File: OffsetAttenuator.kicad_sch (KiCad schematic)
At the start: 15 parts, among them J1 Conn_Coaxial, J2 Conn_Coaxial, SW1 SW_SPST, U1 L7805, X1 CXO_DIP14

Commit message: updating schematic
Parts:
- added D2: LED, symbol Device:LED
- added R5: 220, symbol Device:R
- BT1: value Battery -> Battery 9V
- C1, C2: value C -> 470pF
- C3: value C -> .0047uF
- R1, R3: value R -> 2.2K
- R4: value R -> 4.7K
- RV1: value R_Potentiometer -> 5K
- X1: value CXO_DIP14 -> 4MHz
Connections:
- net GND: now also D2.1 (K)
- net +5V: now reaches U1.3 (OUT), X1.14 (Vcc)
- net +5V: now also R5.2
- net at R4.1, SW1.2 (B): now also U1.1 (IN)
- new net: D2.2 (A), R5.1
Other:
- note added: "Circuit borrowed from this project: https://www.w9dup.org/test_eqpt_files/attenuator_project_2010_may.pdf"

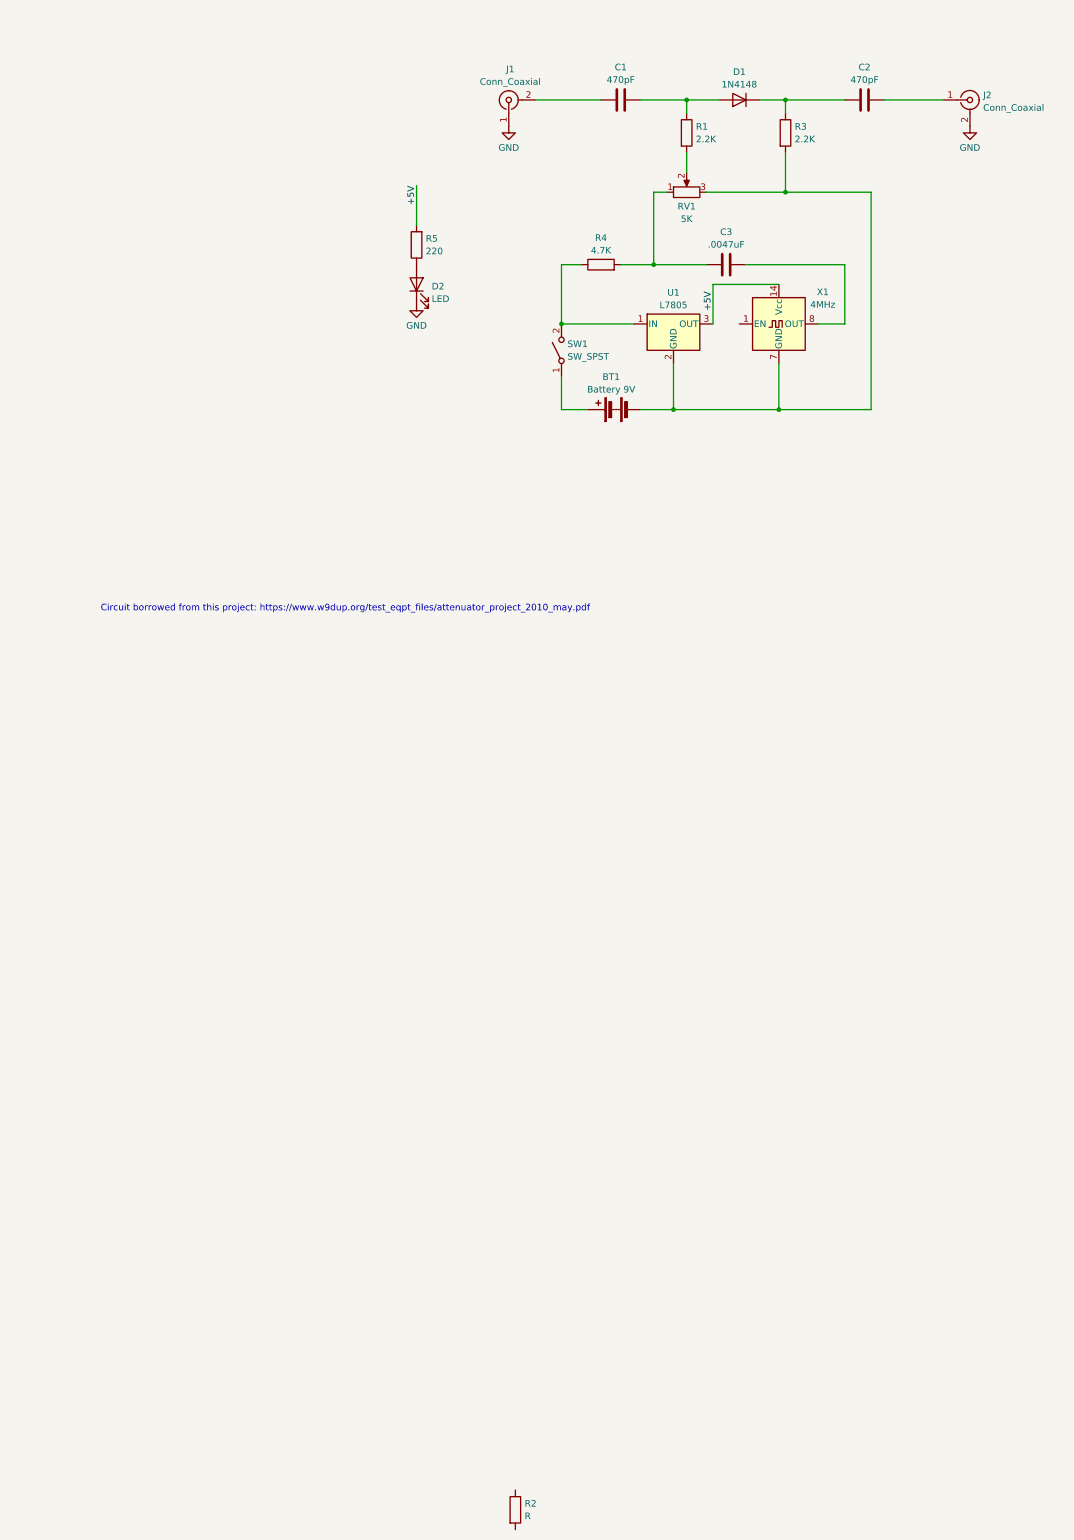
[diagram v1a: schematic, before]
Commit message: adding bypass toggle
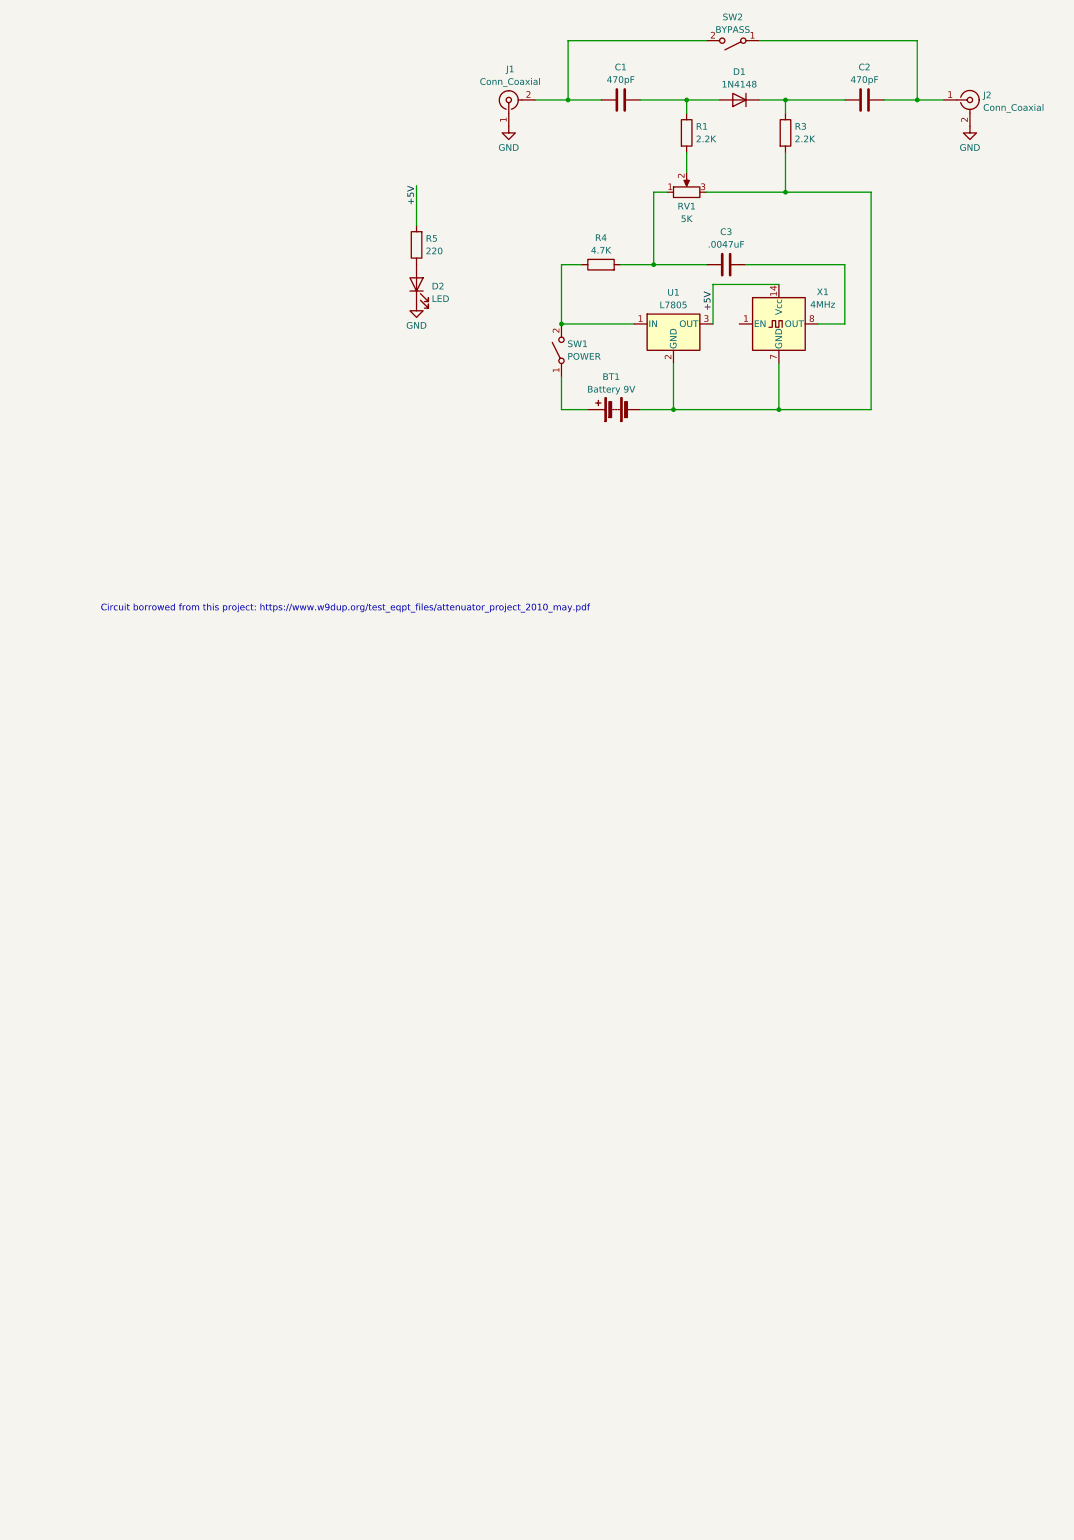
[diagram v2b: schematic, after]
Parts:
- removed R2: R, symbol Device:R
- added SW2: BYPASS, symbol Switch:SW_SPST
- SW1: value SW_SPST -> POWER
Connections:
- net at C2.2, J2.1 (In): now also SW2.1 (A)
- net at C1.1, J1.2 (Ext): now also SW2.2 (B)
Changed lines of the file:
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@@
+	)
+	(junction
+		(at 110.49 95.25)
+		(diameter 0)
+		(color 0 0 0 0)
 	)
 	(junction
@@
 	)
 	(junction
+		(at 177.8 95.25)
+		(diameter 0)
+		(color 0 0 0 0)
+	)
+	(junction
 		(at 151.13 154.94)
 		(diameter 0)
@@
 	(wire
 		(pts
+			(xy 137.16 83.82) (xy 110.49 83.82)
+		)
+		(stroke
+			(width 0)
+			(type default)
+		)
+	)
+	(wire
+		(pts
+			(xy 177.8 95.25) (xy 182.88 95.25)
+		)
+		(stroke
+			(width 0)
+			(type default)
+		)
+	)
+	(wire
+		(pts
 			(xy 127 127) (xy 137.16 127)
 		)
@@
 	(wire
 		(pts
-			(xy 104.14 95.25) (xy 116.84 95.25)
+			(xy 104.14 95.25) (xy 110.49 95.25)
 		)
 		(stroke
@@
 	(wire
 		(pts
+			(xy 110.49 95.25) (xy 116.84 95.25)
+		)
+		(stroke
+			(width 0)
+			(type default)
+		)
+	)
+	(wire
+		(pts
 			(xy 113.03 127) (xy 109.22 127)
 		)
@@
 	(wire
 		(pts
-			(xy 171.45 95.25) (xy 182.88 95.25)
+			(xy 177.8 83.82) (xy 177.8 95.25)
+		)
+		(stroke
+			(width 0)
+			(type default)
+		)
+	)
+	(wire
+		(pts
+			(xy 171.45 95.25) (xy 177.8 95.25)
 		)
 		(stroke
@@
 	(wire
 		(pts
+			(xy 147.32 83.82) (xy 177.8 83.82)
+		)
+		(stroke
+			(width 0)
+			(type default)
+		)
+	)
+	(wire
+		(pts
 			(xy 127 113.03) (xy 127 127)
 		)
@@
 		(pts
 			(xy 151.13 154.94) (xy 168.91 154.94)
+		)
+		(stroke
+			(width 0)
+			(type default)
+		)
+	)
+	(wire
+		(pts
+			(xy 110.49 83.82) (xy 110.49 95.25)
 		)
 		(stroke
@@
 	)
 	(symbol
+		(lib_id "Switch:SW_SPST")
+		(at 142.24 83.82 180)
+		(unit 1)
+		(exclude_from_sim no)
+		(in_bom yes)
+		(on_board yes)
+		(dnp no)
+		(fields_autoplaced yes)
+		(property "Reference" "SW2"
+			(at 142.24 79.2945 0)
+			(effects
+				(font
+					(size 1.27 1.27)
+				)
+			)
+		)
+		(property "Value" "BYPASS"
+			(at 142.24 81.7188 0)
+			(effects
+				(font
+					(size 1.27 1.27)
+				)
+			)
+		)
+		(property "Footprint" ""
+			(at 142.24 83.82 0)
+			(effects
+				(font
+					(size 1.27 1.27)
+				)
+				(hide yes)
+			)
+		)
+		(property "Datasheet" "~"
+			(at 142.24 83.82 0)
+			(effects
+				(font
+					(size 1.27 1.27)
+				)
+				(hide yes)
+			)
+		)
+		(property "Description" "Single Pole Single Throw (SPST) switch"
+			(at 142.24 83.82 0)
+			(effects
+				(font
+					(size 1.27 1.27)
+				)
+				(hide yes)
+			)
+		)
+		(pin "2"
+		)
+		(pin "1"
+		)
+		(instances
+			(project "OffsetAttenuator"
+				(path "/1ad55a5d-7440-488e-8560-ee9e41fda5dc"
+					(reference "SW2")
+					(unit 1)
+				)
+			)
+		)
+	)
+	(symbol
 		(lib_id "Regulator_Linear:L7805")
 		(at 130.81 138.43 0)
@@
 			)
 		)
-		(property "Value" "SW_SPST"
+		(property "Value" "POWER"
 			(at 110.363 144.7221 90)
 			(effects
@@
 					(unit 1)
 				)
-			)
-		)
-	)
-	(symbol
-		(lib_id "Device:R")
-		(at 100.33 367.03 0)
-		(unit 1)
-		(exclude_from_sim no)
-		(in_bom yes)
-		(on_board yes)
-		(dnp no)
-		(fields_autoplaced yes)
-		(property "Reference" "R2"
-			(at 102.108 365.8178 0)
-			(effects
-				(font
-					(size 1.27 1.27)
-				)
-				(justify left)
-			)
-		)
-		(property "Value" "R"
-			(at 102.108 368.2421 0)
-			(effects
-				(font
-					(size 1.27 1.27)
-				)
-				(justify left)
-			)
-		)
-		(property "Footprint" ""
-			(at 98.552 367.03 90)
-			(effects
-				(font
-					(size 1.27 1.27)
-				)
-				(hide yes)
-			)
-		)
-		(property "Datasheet" "~"
-			(at 100.33 367.03 0)
-			(effects
-				(font
-					(size 1.27 1.27)
-				)
-				(hide yes)
-			)
-		)
-		(property "Description" "Resistor"
-			(at 100.33 367.03 0)
-			(effects
-				(font
-					(size 1.27 1.27)
-				)
-				(hide yes)
-			)
-		)
-		(pin "2"
-		)
-		(pin "1"
-		)
-		(instances
-			(project "OffsetAttenuator"
-				(path "/1ad55a5d-7440-488e-8560-ee9e41fda5dc"
-					(reference "R2")
-					(unit 1)
-				)

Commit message: assigning footprints
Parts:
- BT1: footprint (none) -> Connector_PinHeader_2.54mm:PinHeader_1x02_P2.54mm_Vertical
- C1, C2, C3: footprint (none) -> Capacitor_THT:C_Disc_D5.0mm_W2.5mm_P5.00mm
- D2: footprint (none) -> LED_THT:LED_D5.0mm
- J1, J2: footprint (none) -> Library:CONBNC002
- R1, R3, R4, R5: footprint (none) -> Resistor_THT:R_Axial_DIN0309_L9.0mm_D3.2mm_P12.70mm_Horizontal
- U1: footprint (none) -> Package_TO_SOT_THT:TO-220-3_Vertical
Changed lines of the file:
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@@
 			)
 		)
-		(property "Footprint" ""
+		(property "Footprint" "LED_THT:LED_D5.0mm"
 			(at 81.28 130.81 0)
 			(effects
@@
 			)
 		)
-		(property "Footprint" ""
+		(property "Footprint" "Resistor_THT:R_Axial_DIN0309_L9.0mm_D3.2mm_P12.70mm_Horizontal"
 			(at 83.058 123.19 90)
 			(effects
@@
 			)
 		)
-		(property "Footprint" ""
+		(property "Footprint" "Resistor_THT:R_Axial_DIN0309_L9.0mm_D3.2mm_P12.70mm_Horizontal"
 			(at 150.622 101.6 90)
 			(effects
@@
 			)
 		)
-		(property "Footprint" ""
+		(property "Footprint" "Capacitor_THT:C_Disc_D5.0mm_W2.5mm_P5.00mm"
 			(at 144.78 126.0348 0)
 			(effects
@@
 			)
 		)
-		(property "Footprint" ""
+		(property "Footprint" "Capacitor_THT:C_Disc_D5.0mm_W2.5mm_P5.00mm"
 			(at 171.45 94.2848 0)
 			(effects
@@
 			)
 		)
-		(property "Footprint" ""
+		(property "Footprint" "Connector_PinHeader_2.54mm:PinHeader_1x02_P2.54mm_Vertical"
 			(at 117.856 154.94 90)
 			(effects
@@
 			)
 		)
-		(property "Footprint" ""
+		(property "Footprint" "Resistor_THT:R_Axial_DIN0309_L9.0mm_D3.2mm_P12.70mm_Horizontal"
 			(at 116.84 128.778 90)
 			(effects
@@
 			)
 		)
-		(property "Footprint" ""
+		(property "Footprint" "Library:CONBNC002"
 			(at 99.06 95.25 0)
 			(effects
@@
 			)
 		)
-		(property "Footprint" ""
+		(property "Footprint" "Resistor_THT:R_Axial_DIN0309_L9.0mm_D3.2mm_P12.70mm_Horizontal"
 			(at 131.572 101.6 90)
 			(effects
@@
 			)
 		)
-		(property "Footprint" ""
+		(property "Footprint" "Capacitor_THT:C_Disc_D5.0mm_W2.5mm_P5.00mm"
 			(at 124.46 94.2848 0)
 			(effects
@@
 			)
 		)
-		(property "Footprint" ""
+		(property "Footprint" "Package_TO_SOT_THT:TO-220-3_Vertical"
 			(at 131.445 142.24 0)
 			(effects
@@
 			)
 		)
-		(property "Footprint" ""
+		(property "Footprint" "Library:CONBNC002"
 			(at 187.96 95.25 0)
 			(effects

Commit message: upgrading to kicad 9
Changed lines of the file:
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@@
 (kicad_sch
-	(version 20231120)
+	(version 20250114)
 	(generator "eeschema")
-	(generator_version "8.0")
+	(generator_version "9.0")
 	(paper "A4")
+	(text "Circuit borrowed from this project: https://www.w9dup.org/test_eqpt_files/attenuator_project_2010_may.pdf"
+		(exclude_from_sim no)
+		(at 67.564 193.294 0)
+		(effects
+			(font
+				(size 1.27 1.27)
+			)
+		)
+	)
 	(junction
 		(at 133.35 95.25)
@@
 		)
 	)
-	(text "Circuit borrowed from this project: https://www.w9dup.org/test_eqpt_files/attenuator_project_2010_may.pdf"
-		(exclude_from_sim no)
-		(at 67.564 193.294 0)
+	(label "+5V"
+		(at 81.28 111.76 270)
 		(effects
 			(font
 				(size 1.27 1.27)
 			)
+			(justify right bottom)
 		)
 	)
 	(label "+5V"
-		(at 81.28 111.76 270)
-		(fields_autoplaced yes)
+		(at 138.43 135.89 90)
 		(effects
 			(font
 				(size 1.27 1.27)
 			)
-			(justify right bottom)
-		)
-	)
-	(label "+5V"
-		(at 138.43 135.89 90)
-		(fields_autoplaced yes)
-		(effects
-			(font
-				(size 1.27 1.27)
-			)
 			(justify left bottom)
 		)
@@
 		)
 	)
+	(embedded_fonts no)
 )

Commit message: adding footprints and models
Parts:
- BT1: footprint Connector_PinHeader_2.54mm:PinHeader_1x02_P2.54mm_Vertical -> Library:1294PCB_29P57X53P85_KEY
- RV1: footprint (none) -> Library:TRIM_3310Y-001-502L
- SW1, SW2: footprint (none) -> Library:SWT3
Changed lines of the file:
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@@
 			)
 		)
-		(property "Footprint" ""
+		(property "Footprint" "Library:TRIM_3310Y-001-502L"
 			(at 133.35 113.03 0)
 			(effects
@@
 			)
 		)
-		(property "Footprint" "Connector_PinHeader_2.54mm:PinHeader_1x02_P2.54mm_Vertical"
+		(property "Footprint" "Library:1294PCB_29P57X53P85_KEY"
 			(at 117.856 154.94 90)
 			(effects
@@
 			)
 		)
-		(property "Footprint" ""
+		(property "Footprint" "Library:SWT3"
 			(at 142.24 83.82 0)
 			(effects
@@
 			)
 		)
-		(property "Footprint" ""
+		(property "Footprint" "Library:SWT3"
 			(at 109.22 143.51 0)
 			(effects

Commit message: schematic updates
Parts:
- X1: footprint Oscillator:Oscillator_DIP-14 -> Library:OSC_ECS-2100AX-040
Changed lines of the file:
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@@
 			)
 		)
-		(property "Footprint" "Oscillator:Oscillator_DIP-14"
+		(property "Footprint" "Library:OSC_ECS-2100AX-040"
 			(at 162.56 147.32 0)
 			(effects
